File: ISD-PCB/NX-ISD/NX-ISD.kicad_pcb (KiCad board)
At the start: 4 copper layers, 77 x 48.6 mm, 96 parts, among them J1 1-2328702-0, P1 S2B-PH-SM4-TB, Q1 AO3400A, Q2 AO3401A, Q3 BC847W, Q4 AO3400A, U1 ESP32-S3-WROOM-1, U10 BNO085, U11 HYCW275-USBC24-050B, U12 OPT3001DNPR, U13 RT9193-18GB, U14 ZDSD02GLGEAG, U15 USBLC6-2P6, U2 TLV62568DBV, U3 MAX17048G_T10, U4 RV-3028-C7, U5 MAX30102, U6 BME690, U7 TM-2025A, U8 BQ25170DSGR, U9 RT9193-28GB, Y2 32.768

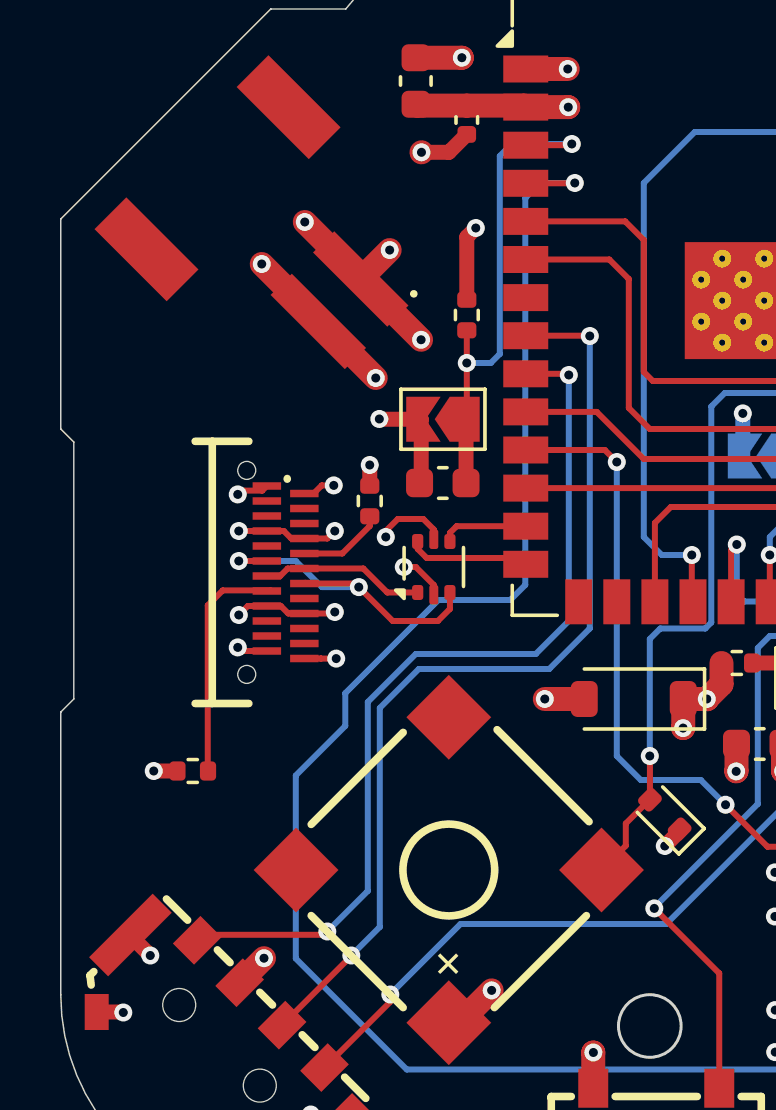
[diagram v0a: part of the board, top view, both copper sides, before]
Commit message: new USBC plug and minor changes to ISD-Core
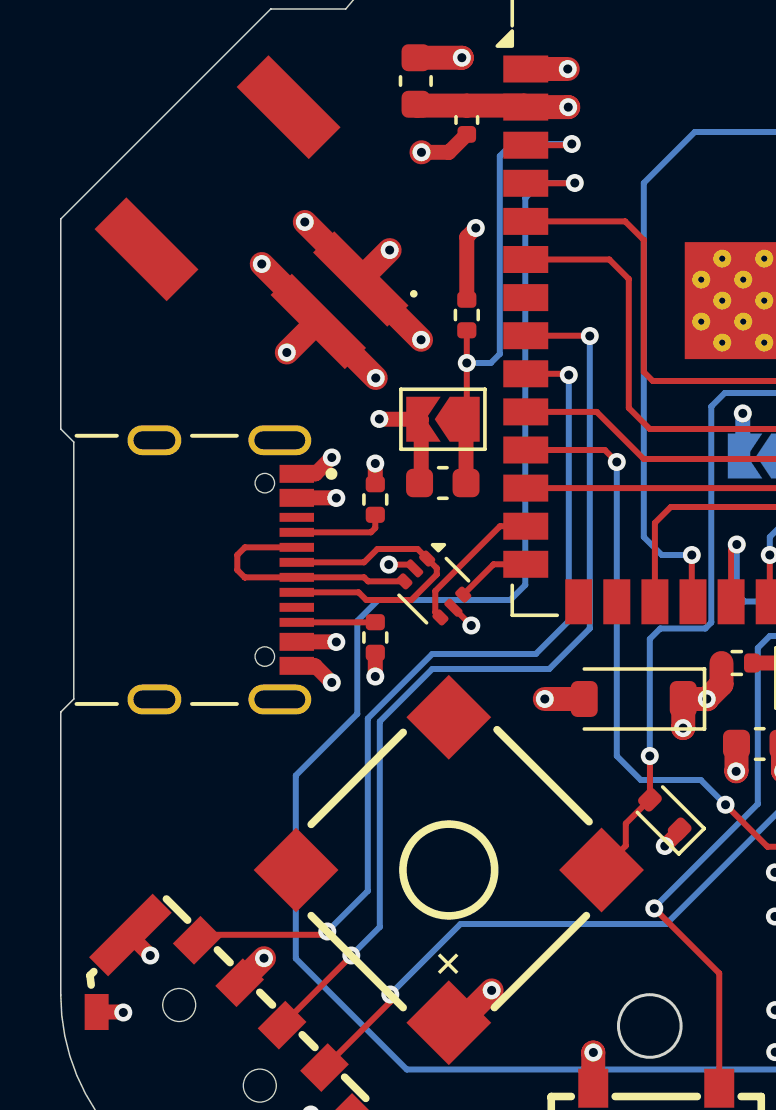
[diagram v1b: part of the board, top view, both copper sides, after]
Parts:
- removed U11: HYCW275-USBC24-050B, Global Footprints:USB-C-SMD_HYCW275-USBC24-050B
- added J2: UJ20-C-H-G-SMT-1-P16-TR, NX-AW-footprints:SAMESKY_UJ20-C-H-G-SMT-1-P16-TR, F.Cu at (112.9, 102.8)
- moved R9 7.54 mm to (122.8, 105.0), turned to -90 degrees
- moved U15 0.70 mm to (124.8, 103.4), turned to -45 degrees
- moved R1 0.19 mm to (122.8, 100.5)
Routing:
- net /Power section/USB_P: track 10.6 -> 4.80 mm, vias 6 -> 4
- net /Power section/CC2: track 7.97 -> 2.62 mm
- net /Power section/U_D+: track 5.46 -> 10.5 mm
- net /Power section/U_D-: track 11.4 -> 8.32 mm, vias 2 -> 0
- net /Logic section/D-: track 2.91 -> 4.86 mm
- net /Logic section/!ALERT: track 88.0 -> 89.2 mm
- net /Logic section/D+: track 4.08 -> 3.12 mm
- net GND: track 97.3 -> 96.6 mm, vias 98 -> 97

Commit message: v1p3 major fix rework in progress
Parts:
- added C2: 100n, Capacitor_SMD:C_0402_1005Metric, F.Cu at (185.7, 96.7)
- added C24: 100n, Capacitor_SMD:C_0402_1005Metric, F.Cu at (163.3, 109.5)
- added C25: 100n, Capacitor_SMD:C_0402_1005Metric, F.Cu at (170.2, 109.5)
- added R21: 4.7k, Resistor_SMD:R_0402_1005Metric, F.Cu at (180.1, 109.2)
- added R22: 4.7k, Resistor_SMD:R_0402_1005Metric, F.Cu at (181.4, 115.8)
- added R23: 4.7k, Resistor_SMD:R_0402_1005Metric, F.Cu at (180.2, 115.8)
- added R24: 200k, Resistor_SMD:R_0402_1005Metric, F.Cu at (176.5, 115.8)
- added U11: PCA9306, Package_SO:VSSOP-8_2.3x2mm_P0.5mm, F.Cu at (177.9, 113.3)
- added U16: TXB0106RGY, Package_DFN_QFN:Texas_RGY_R-PVQFN-N16_EP2.05x2.55mm, F.Cu at (166.7, 107.3)
- R11: value 500 -> 499
- R2: value 3K3 -> 499
- moved C12 0.29 mm to (186.6, 100.8)
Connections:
- D1 pad 1: GND -> /Logic section/BAT_STAT
- J1 pad 2: /Logic section/DC -> /Peripherie/LOW_DC
- J1 pad 3: /Logic section/CS_TFT -> /Peripherie/LOW_CS_TFT
- J1 pad 4: /Logic section/SCK -> /Peripherie/LOW_SCK
- J1 pad 5: /Logic section/MOSI -> /Peripherie/LOW_MOSI
- J1 pad 6: /Logic section/RST -> /Peripherie/LOW_RST
- R2 pad 1: VBUS -> +3V3
- RN1 pad 3: /Logic section/!INT_HR -> /Logic section/!ALERT
- U3 pad 10: GND -> (no net)
- U3 pad 11: GND -> (no net)
- U5 pad 2: /Logic section/SCL_1 -> Net-(U11-SCL1)
- U5 pad 3: /Logic section/SDA_1 -> Net-(U11-SDA1)
- U8 pad 10: GND -> (no net)
- U8 pad 11: GND -> (no net)
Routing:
- net /Logic section/!ALERT: track 89.2 -> 111.6 mm, vias 2 -> 3
- net /Logic section/SDA_1: track 148.8 -> 130.2 mm, vias 9 -> 7
- net /Peripherie/LOW_RST: track 0.00 -> 15.1 mm, vias 0 -> 2
- net /Peripherie/LOW_CS_TFT: track 0.00 -> 15.0 mm, vias 0 -> 2
- net /Peripherie/LOW_SCK: track 0.00 -> 12.4 mm, vias 0 -> 2
- net Net-(U11-SCL1): track 0.00 -> 11.4 mm
- net /Peripherie/LOW_MOSI: track 0.00 -> 10.9 mm, vias 0 -> 2
- net Net-(U11-SDA1): track 0.00 -> 10.8 mm
- net /Logic section/SCL_1: track 143.9 -> 133.9 mm, vias 9 -> 8
- net /Logic section/DC: track 27.9 -> 37.5 mm
- net GND: track 96.6 -> 106.1 mm, vias 97 -> 103
- net /Peripherie/LOW_DC: track 0.00 -> 8.22 mm, vias 0 -> 2
- net /Logic section/RST: track 19.5 -> 26.3 mm
- net /Logic section/CS_TFT: track 24.2 -> 30.4 mm
- net +1V8: track 5.38 -> 9.18 mm, vias 3 -> 7
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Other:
- board text added: "v1p3"
- board text removed: "v1p1"

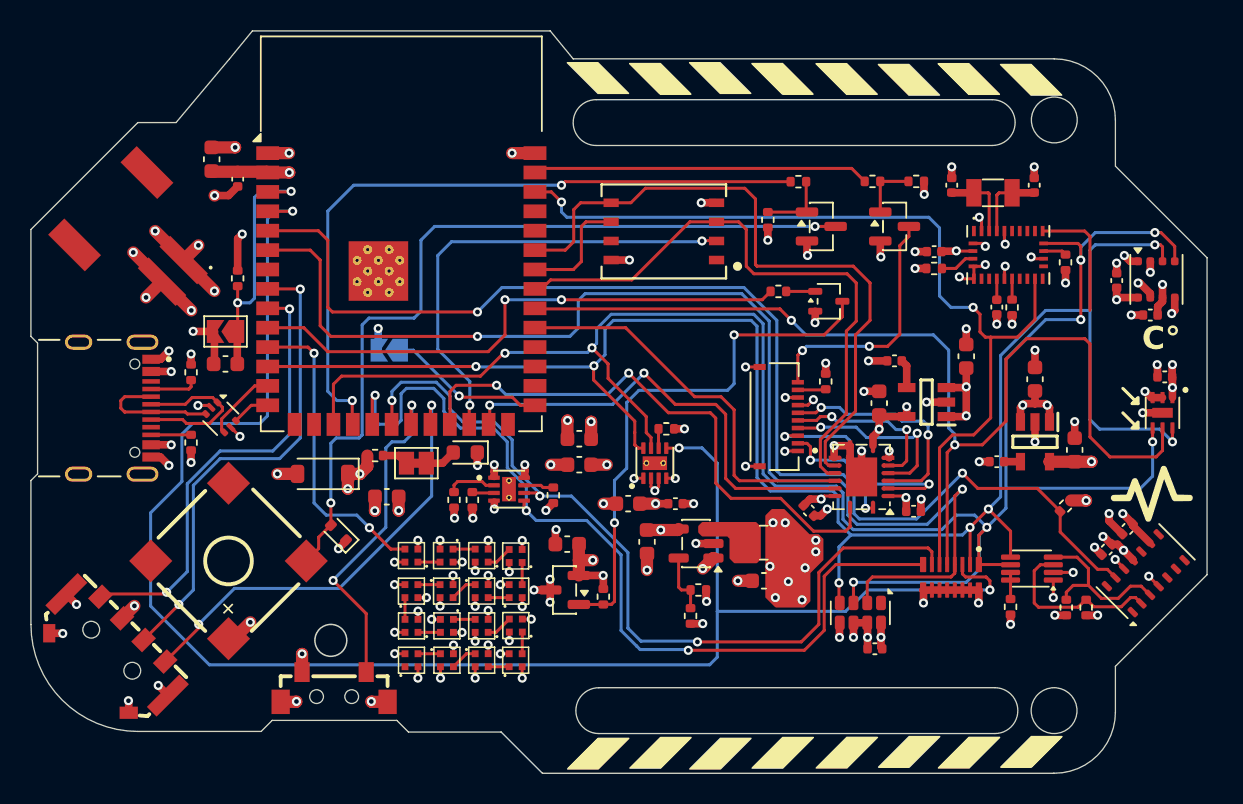
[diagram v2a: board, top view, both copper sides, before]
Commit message: v1p3 : Fixed LED & DRC check successful
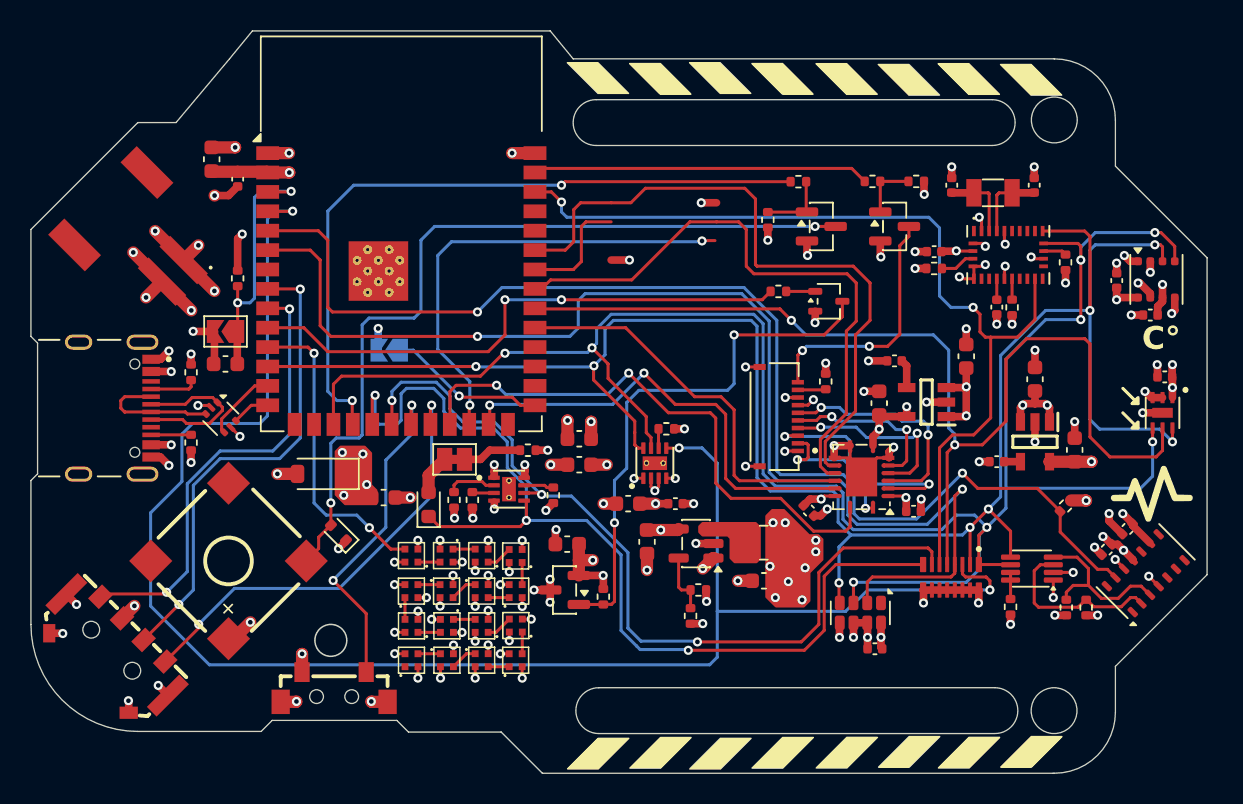
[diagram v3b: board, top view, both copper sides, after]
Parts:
- removed U14: ZDSD02GLGEAG, NX-AW-footprints:LGA-8_L8.0-W6.0-P1.27-TL_ZDSD02GLGEAG
- R2: value 499 -> 220
- moved R2 10.0 mm to (144.9, 105.5), turned to 180 degrees
- moved D1 4.16 mm to (138.4, 109.1), turned to 90 degrees
- moved JP1 2.51 mm to (140.1, 106.2), turned to 180 degrees
- moved C20 0.22 mm to (135.4, 108.7)
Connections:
- R2 pad 1: +3V3 -> VBAT
- U3 pad 10: (no net) -> GND
- U3 pad 11: (no net) -> GND
- U8 pad 10: (no net) -> GND
- U8 pad 11: (no net) -> GND
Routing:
- net /Logic section/BAT_STAT: track 60.1 -> 67.0 mm, vias 4 -> 3
- net VBUS: track 4.87 -> 0.78 mm, vias 4 -> 5
- net Net-(JP1-A): track 1.75 -> 3.89 mm
- net /Peripherie/LOW_DC: track 8.22 -> 9.59 mm
- net VBAT: track 22.2 -> 23.0 mm, vias 12 -> 13
- net GND: track 106.1 -> 106.8 mm, vias 103 -> 102
- net Net-(D1-A): track 2.05 -> 2.60 mm
- net /Logic section/SDA_1: vias 7 -> 8
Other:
- board text added: "(ON BOT SLKSCRN)"
- board text added: "= CUSTOM QR CODE LOCATION, WHEN USING JLCPCB"
- board text added: "= Display location"

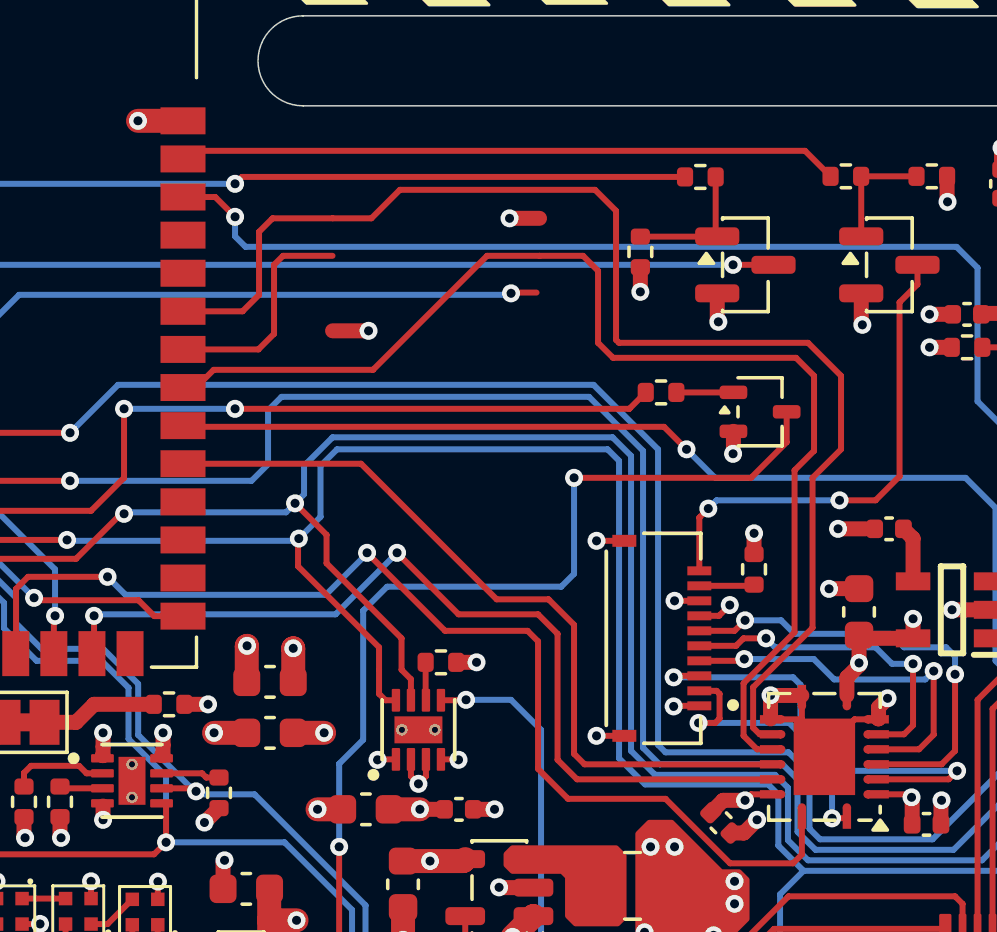
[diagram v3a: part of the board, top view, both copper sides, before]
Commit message: fixed: NAND Flash
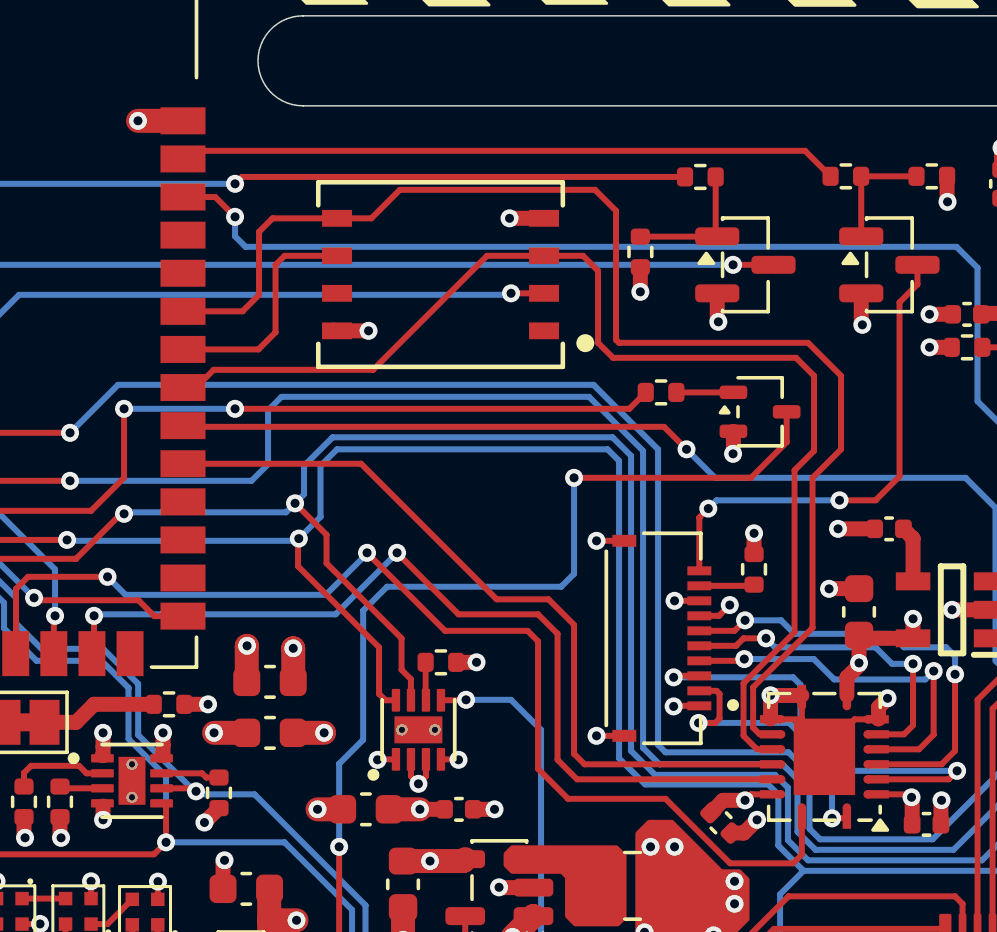
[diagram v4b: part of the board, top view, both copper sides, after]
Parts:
- added U14: ZDSD02GLGEAG, NX-AW-footprints:LGA-8_L8.0-W6.0-P1.27-TL_ZDSD02GLGEAG, F.Cu at (153.9, 91.2)

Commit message: Silkscreen Font change
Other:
- board text added: "3.7V - 4.2V"
- board text added: "CHRG: 600 mA --> 1S LiPo 1200 mAh <--"
- board text removed: "CHRG: 600mA"
- board text removed: "LIPO [1S] 3.7V - 4.2V"

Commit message: Added LiPo polarity mark
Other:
- board text added: "+"
- board text added: "-"
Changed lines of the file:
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@@
+		)
+	)
+	(gr_text "+"
+		(at 122.8 87.1 45)
+		(layer "F.SilkS")
+		(effects
+			(font
+				(face "Circuit Forem")
+				(size 3 3)
+				(thickness 0.25)
+			)
+			(justify bottom mirror)
+		)
+		(render_cache "+" 45
+			(polygon
+				(pts
+					(xy 121.297574 85.181267) (xy 121.631112 85.514805) (xy 121.966075 85.179842) (xy 122.382252 85.59602)
+					(xy 122.047289 85.930983) (xy 122.382252 86.265946) (xy 121.966075 86.682123) (xy 121.631112 86.347161)
+					(xy 121.296019 86.682253) (xy 120.879842 86.266075) (xy 121.214934 85.930983) (xy 120.881396 85.597445)
+				)
+			)
 		)
 	)
@@
 				)
 			)
+		)
+	)
+	(gr_text "-"
+		(at 116.15 92.05 45)
+		(layer "B.SilkS")
+		(effects
+			(font
+				(face "Circuit Forem")
+				(size 3 3)
+				(thickness 0.25)
+			)
+			(justify bottom mirror)
+		)
+		(render_cache "-" 45
+			(polygon
+				(pts
+					(xy 115.732252 90.54602) (xy 115.316075 90.129842) (xy 114.229842 91.216075) (xy 114.646019 91.632253)
+				)
+			)
+		)
+	)
+	(gr_text "+"
+		(at 120.15 88.2 45)
+		(layer "B.SilkS")
+		(effects
+			(font
+				(face "Circuit Forem")
+				(size 3 3)
+				(thickness 0.25)
+			)
+			(justify bottom mirror)
+		)
+		(render_cache "+" 45
+			(polygon
+				(pts
+					(xy 118.647574 86.281267) (xy 118.981112 86.614805) (xy 119.316075 86.279842) (xy 119.732252 86.69602)
+					(xy 119.397289 87.030983) (xy 119.732252 87.365946) (xy 119.316075 87.782123) (xy 118.981112 87.447161)
+					(xy 118.646019 87.782253) (xy 118.229842 87.366075) (xy 118.564934 87.030983) (xy 118.231396 86.697445)
+				)
+			)

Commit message: Added 3D-Renders to README
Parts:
- G10, G11, G12, G13, G14, G15, G16: footprint NX-AW-footprints:LED-SMD_4P-L1.0-W1.0-TL_XL-1010RGBC-WS2812B -> Global Footprints:LED-SMD_4P-L1.0-W1.0-TL_XL-1010RGBC-WS2812B
- J2: footprint NX-AW-footprints:SAMESKY_UJ20-C-H-G-SMT-1-P16-TR -> Global Footprints:SAMESKY_UJ20-C-H-G-SMT-1-P16-TR
- U12: footprint NX-AW-footprints:SON65P200X200X65-7N -> Global Footprints:SON65P200X200X65-7N
